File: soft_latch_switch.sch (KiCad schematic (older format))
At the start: 8 parts, among them J9 Conn_01x05, Q1 SI01P10, Q2 MMBT5551L

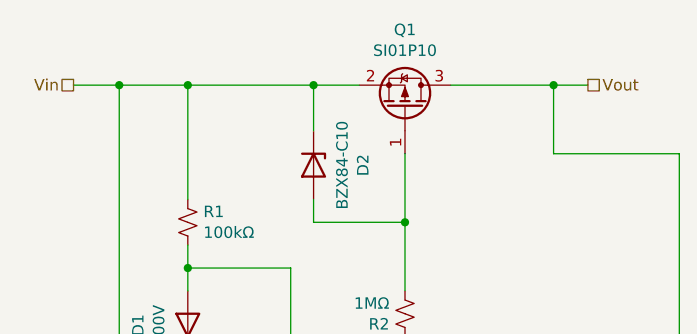
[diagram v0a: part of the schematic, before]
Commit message: alternate component values added
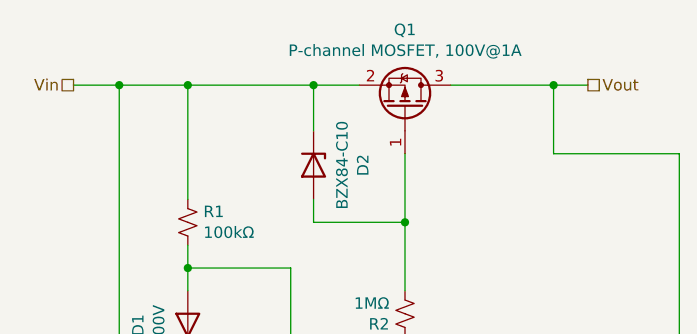
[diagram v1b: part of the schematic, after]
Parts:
- Q1: value SI01P10 -> P-channel MOSFET, 100V@1A; 100V Values (none) -> SI01P10, PMV240SPR; 80V Values (none) -> SI2387DS, SI2337DS, SQ2337ES
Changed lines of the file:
@@
 Vout
-$Comp
-L Transistor_FET:AO3401A Q1
-U 1 1 61766161
-P 6250 3500
-AR Path="/6173FDB3/61766161" Ref="Q1"  Part="1"
-AR Path="/61742C5F/61766161" Ref="Q3"  Part="1"
-AR Path="/615B14D6/61766161" Ref="Q1"  Part="1"
-F 0 "Q1" V 6592 3500 50  0000 C CNN
-F 1 "SI01P10" V 6501 3500 50  0000 C CNN
-F 2 "Package_TO_SOT_SMD:SOT-23" H 6450 3425 50  0001 L CIN
-F 3 "https://www.mccsemi.com/pdf/Products/SI01P10(SOT-23).pdf" H 6250 3500 50  0001 L CNN
-	1    6250 3500
-	0    1    -1   0
-$EndComp
 $Comp
 L Device:R_Small_US R?
@@
 	0    1    1    0
 $EndComp
+$Comp
+L Transistor_FET:AO3401A Q1
+U 1 1 61766161
+P 6250 3500
+AR Path="/6173FDB3/61766161" Ref="Q1"  Part="1"
+AR Path="/61742C5F/61766161" Ref="Q3"  Part="1"
+AR Path="/615B14D6/61766161" Ref="Q1"  Part="1"
+F 0 "Q1" V 6592 3500 50  0000 C CNN
+F 1 "P-channel MOSFET, 100V@1A" V 6501 3500 50  0000 C CNN
+F 2 "Package_TO_SOT_SMD:SOT-23" H 6450 3425 50  0001 L CIN
+F 3 "https://www.mccsemi.com/pdf/Products/SI01P10(SOT-23).pdf" H 6250 3500 50  0001 L CNN
+F 4 "SI01P10, PMV240SPR" V 6250 3500 50  0001 C CNN "100V Values"
+F 5 "SI2387DS, SI2337DS, SQ2337ES" V 6250 3500 50  0001 C CNN "80V Values"
+	1    6250 3500
+	0    1    -1   0
+$EndComp
 $EndSCHEMATC

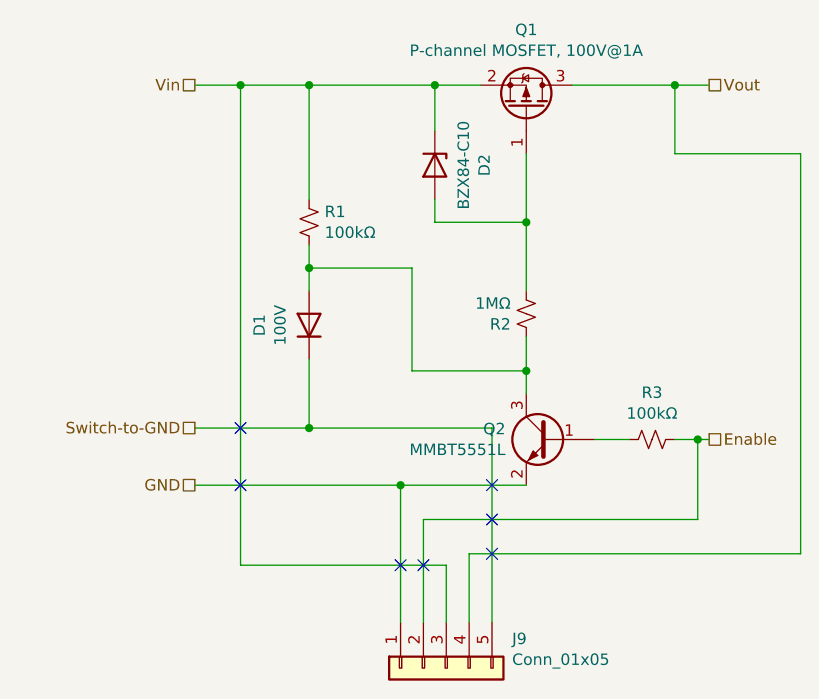
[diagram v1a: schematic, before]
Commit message: schematic update
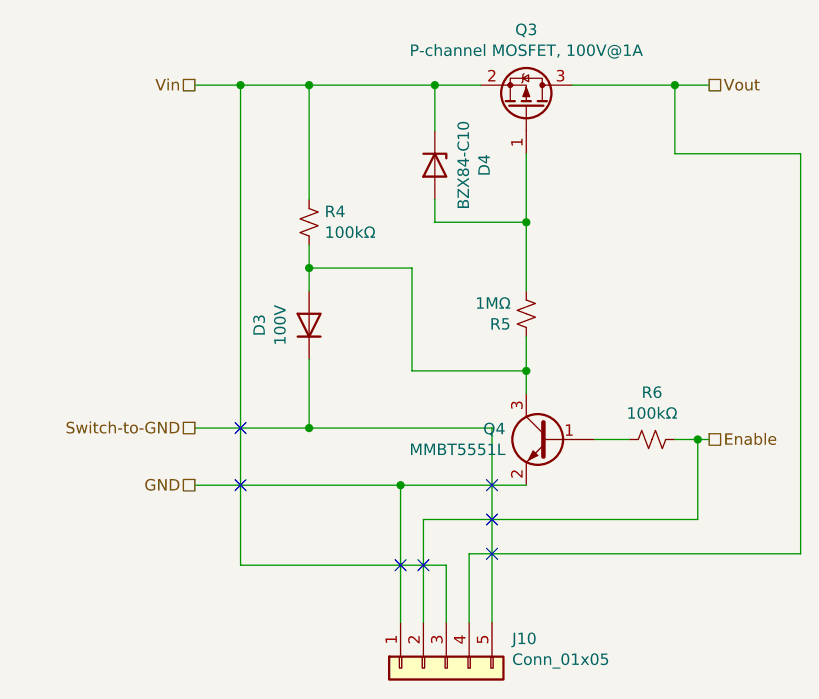
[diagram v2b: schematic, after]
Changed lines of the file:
@@
 $Descr A4 11693 8268
 encoding utf-8
-Sheet 2 9
+Sheet 3 9
 Title ""
 Date ""
@@
 AR Path="/61742C5F/61740EC7" Ref="R4"  Part="1"
 AR Path="/615B14D6/61740EC7" Ref="R1"  Part="1"
-F 0 "R1" H 5368 4046 50  0000 L CNN
+F 0 "R4" H 5368 4046 50  0000 L CNN
 F 1 "100kΩ" H 5368 3955 50  0000 L CNN
 F 2 "Resistor_SMD:R_0805_2012Metric" H 5300 4000 50  0001 C CNN
@@
 AR Path="/61742C5F/61740ED3" Ref="D3"  Part="1"
 AR Path="/615B14D6/61740ED3" Ref="D1"  Part="1"
-F 0 "D1" H 5300 4667 50  0000 C CNN
+F 0 "D3" H 5300 4667 50  0000 C CNN
 F 1 "100V" H 5300 4576 50  0000 C CNN
 F 2 "Diode_SMD:D_SOT-23_ANK" H 5300 4450 50  0001 C CNN
@@
 AR Path="/61742C5F/6159F419" Ref="R5"  Part="1"
 AR Path="/615B14D6/6159F419" Ref="R2"  Part="1"
-F 0 "R2" H 6318 4446 50  0000 L CNN
+F 0 "R5" H 6318 4446 50  0000 L CNN
 F 1 "1MΩ" H 6318 4355 50  0000 L CNN
 F 2 "Resistor_SMD:R_0805_2012Metric" H 6250 4400 50  0001 C CNN
@@
 AR Path="/61742C5F/6175BFA3" Ref="Q4"  Part="1"
 AR Path="/615B14D6/6175BFA3" Ref="Q2"  Part="1"
-F 0 "Q2" H 6541 4996 50  0000 L CNN
+F 0 "Q4" H 6541 4996 50  0000 L CNN
 F 1 "MMBT5551L" H 6541 4905 50  0000 L CNN
 F 2 "Package_TO_SOT_SMD:SOT-23" H 6550 4875 50  0001 L CIN
@@
 AR Path="/61742C5F/6158D7E7" Ref="D4"  Part="1"
 AR Path="/615B14D6/6158D7E7" Ref="D2"  Part="1"
-F 0 "D2" H 5850 3967 50  0000 C CNN
+F 0 "D4" H 5850 3967 50  0000 C CNN
 F 1 "BZX84-C10" H 5850 3876 50  0000 C CNN
 F 2 "Diode_SMD:D_SOT-23_ANK" H 5850 3750 50  0001 C CNN
@@
 AR Path="/6173FDB3/615AB3CA" Ref="J9"  Part="1"
 AR Path="/61742C5F/615AB3CA" Ref="J10"  Part="1"
-F 0 "J9" V 5772 5662 50  0000 R CNN
+F 0 "J10" V 5772 5662 50  0000 R CNN
 F 1 "Conn_01x05" V 5863 5662 50  0000 R CNN
 F 2 "Connector_PinHeader_2.54mm:PinHeader_1x05_P2.54mm_Vertical" H 5900 5950 50  0001 C CNN
@@
 AR Path="/61742C5F/61740EEC" Ref="R6"  Part="1"
 AR Path="/615B14D6/61740EEC" Ref="R3"  Part="1"
-F 0 "R3" V 6595 4950 50  0000 C CNN
+F 0 "R6" V 6595 4950 50  0000 C CNN
 F 1 "100kΩ" V 6686 4950 50  0000 C CNN
 F 2 "Resistor_SMD:R_0805_2012Metric" H 6800 4950 50  0001 C CNN
@@
 AR Path="/61742C5F/61766161" Ref="Q3"  Part="1"
 AR Path="/615B14D6/61766161" Ref="Q1"  Part="1"
-F 0 "Q1" V 6592 3500 50  0000 C CNN
+F 0 "Q3" V 6592 3500 50  0000 C CNN
 F 1 "P-channel MOSFET, 100V@1A" V 6501 3500 50  0000 C CNN
 F 2 "Package_TO_SOT_SMD:SOT-23" H 6450 3425 50  0001 L CIN

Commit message: schematic cleanup
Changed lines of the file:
@@
 $Descr A4 11693 8268
 encoding utf-8
-Sheet 3 9
+Sheet 9 9
 Title ""
 Date ""
@@
 AR Path="/61742C5F/61740EC7" Ref="R4"  Part="1"
 AR Path="/615B14D6/61740EC7" Ref="R1"  Part="1"
-F 0 "R4" H 5368 4046 50  0000 L CNN
+F 0 "R1" H 5368 4046 50  0000 L CNN
 F 1 "100kΩ" H 5368 3955 50  0000 L CNN
 F 2 "Resistor_SMD:R_0805_2012Metric" H 5300 4000 50  0001 C CNN
@@
 AR Path="/61742C5F/61740ED3" Ref="D3"  Part="1"
 AR Path="/615B14D6/61740ED3" Ref="D1"  Part="1"
-F 0 "D3" H 5300 4667 50  0000 C CNN
+F 0 "D1" H 5300 4667 50  0000 C CNN
 F 1 "100V" H 5300 4576 50  0000 C CNN
 F 2 "Diode_SMD:D_SOT-23_ANK" H 5300 4450 50  0001 C CNN
@@
 AR Path="/61742C5F/6159F419" Ref="R5"  Part="1"
 AR Path="/615B14D6/6159F419" Ref="R2"  Part="1"
-F 0 "R5" H 6318 4446 50  0000 L CNN
+F 0 "R2" H 6318 4446 50  0000 L CNN
 F 1 "1MΩ" H 6318 4355 50  0000 L CNN
 F 2 "Resistor_SMD:R_0805_2012Metric" H 6250 4400 50  0001 C CNN
@@
 AR Path="/61742C5F/6175BFA3" Ref="Q4"  Part="1"
 AR Path="/615B14D6/6175BFA3" Ref="Q2"  Part="1"
-F 0 "Q4" H 6541 4996 50  0000 L CNN
+F 0 "Q2" H 6541 4996 50  0000 L CNN
 F 1 "MMBT5551L" H 6541 4905 50  0000 L CNN
 F 2 "Package_TO_SOT_SMD:SOT-23" H 6550 4875 50  0001 L CIN
@@
 AR Path="/61742C5F/6158D7E7" Ref="D4"  Part="1"
 AR Path="/615B14D6/6158D7E7" Ref="D2"  Part="1"
-F 0 "D4" H 5850 3967 50  0000 C CNN
+F 0 "D2" H 5850 3967 50  0000 C CNN
 F 1 "BZX84-C10" H 5850 3876 50  0000 C CNN
 F 2 "Diode_SMD:D_SOT-23_ANK" H 5850 3750 50  0001 C CNN
@@
 AR Path="/6173FDB3/615AB3CA" Ref="J9"  Part="1"
 AR Path="/61742C5F/615AB3CA" Ref="J10"  Part="1"
-F 0 "J10" V 5772 5662 50  0000 R CNN
+F 0 "J9" V 5772 5662 50  0000 R CNN
 F 1 "Conn_01x05" V 5863 5662 50  0000 R CNN
 F 2 "Connector_PinHeader_2.54mm:PinHeader_1x05_P2.54mm_Vertical" H 5900 5950 50  0001 C CNN
@@
 AR Path="/61742C5F/61740EEC" Ref="R6"  Part="1"
 AR Path="/615B14D6/61740EEC" Ref="R3"  Part="1"
-F 0 "R6" V 6595 4950 50  0000 C CNN
+F 0 "R3" V 6595 4950 50  0000 C CNN
 F 1 "100kΩ" V 6686 4950 50  0000 C CNN
 F 2 "Resistor_SMD:R_0805_2012Metric" H 6800 4950 50  0001 C CNN
@@
 AR Path="/61742C5F/61766161" Ref="Q3"  Part="1"
 AR Path="/615B14D6/61766161" Ref="Q1"  Part="1"
-F 0 "Q3" V 6592 3500 50  0000 C CNN
+F 0 "Q1" V 6592 3500 50  0000 C CNN
 F 1 "P-channel MOSFET, 100V@1A" V 6501 3500 50  0000 C CNN
 F 2 "Package_TO_SOT_SMD:SOT-23" H 6450 3425 50  0001 L CIN
